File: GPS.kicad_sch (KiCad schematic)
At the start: 7 parts, among them Q1 BSS138, U46 2.54mm 2x6 socket

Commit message: Prepare v0.2
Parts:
- U13: footprint xtech:UM9XX_WitMotion -> local_Connectors:UM9XX_WitMotion Sabo
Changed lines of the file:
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@@
 	(title_block
 		(title "OpenMower SABO Mainboard for Series I & II")
-		(date "2025-02-26")
-		(rev "v0.1")
+		(date "2025-05-04")
+		(rev "v0.2")
 		(company "Apeheanger <joerg@ebeling.ws> for OpenMower")
 		(comment 1 "This design is licensed under CC BY-NC 4.0")
@@
 			)
 		)
-		(property "Footprint" "xtech:UM9XX_WitMotion"
+		(property "Footprint" "local_Connectors:UM9XX_WitMotion Sabo"
 			(at 184.15 107.95 0)
 			(effects
@@
 		(on_board yes)
 		(dnp no)
-		(fields_autoplaced yes)
 		(property "Reference" "Q1"
 			(at 166.37 106.6799 0)
@@
 		)
 		(property "Value" "BSS138"
-			(at 166.37 109.2199 0)
-			(effects
-				(font
+			(at 164.846 109.474 0)
+			(effects
+				(font

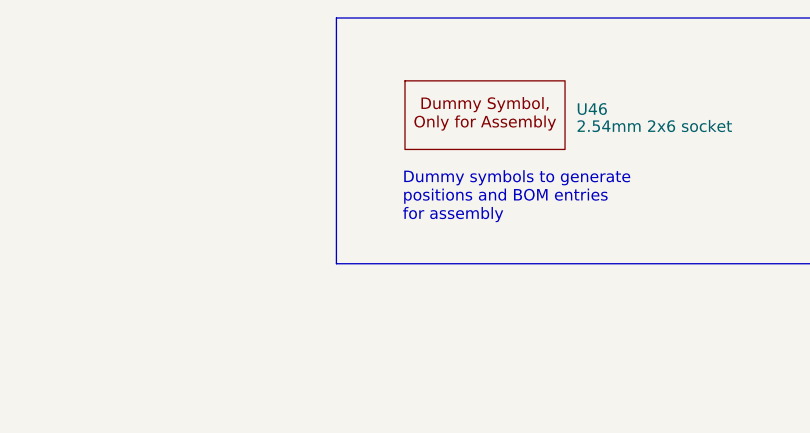
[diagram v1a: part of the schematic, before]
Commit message: Add RoHS Compliance Summary
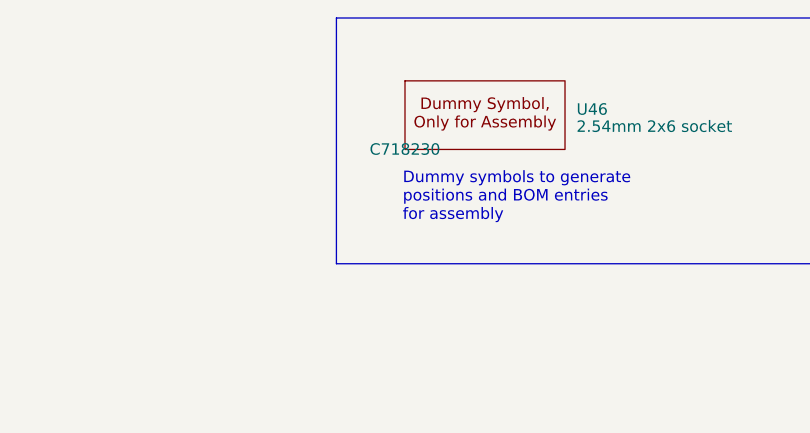
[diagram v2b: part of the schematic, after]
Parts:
- U46: JLC C718230 -> (none); LCSC Part # (none) -> C718230
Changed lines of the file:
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@@
+			)
+		)
+		(property "MPN" ""
+			(at 184.15 107.95 0)
+			(effects
+				(font
+					(size 1.27 1.27)
+				)
 			)
 		)
@@
 			)
 		)
+		(property "MPN" ""
+			(at 217.17 97.79 0)
+			(effects
+				(font
+					(size 1.27 1.27)
+				)
+			)
+		)
 		(pin "1"
 		)
@@
 			)
 		)
+		(property "MPN" ""
+			(at 139.7 115.57 0)
+			(effects
+				(font
+					(size 1.27 1.27)
+				)
+			)
+		)
 		(pin "1"
 		)
@@
 			)
 		)
+		(property "MPN" ""
+			(at 124.46 60.96 0)
+			(effects
+				(font
+					(size 1.27 1.27)
+				)
+			)
+		)
 		(pin "1"
 		)
@@
 			)
 		)
+		(property "MPN" ""
+			(at 147.32 107.95 0)
+			(effects
+				(font
+					(size 1.27 1.27)
+				)
+			)
+		)
 		(pin "1"
 		)
@@
 			)
 		)
-		(property "JLC" "C718230"
+		(property "JLC" ""
 			(at 354.33 31.75 0)
 			(effects
@@
 				)
 				(hide yes)
+			)
+		)
+		(property "MPN" ""
+			(at 354.33 31.75 0)
+			(effects
+				(font
+					(size 1.27 1.27)
+				)
+			)
+		)
+		(property "LCSC Part #" "C718230"
+			(at 354.33 31.75 0)
+			(effects
+				(font
+					(size 1.27 1.27)
+				)
 			)
 		)
@@
 			)
 		)
+		(property "MPN" ""
+			(at 160.02 107.95 0)
+			(effects
+				(font
+					(size 1.27 1.27)
+				)
+			)
+		)

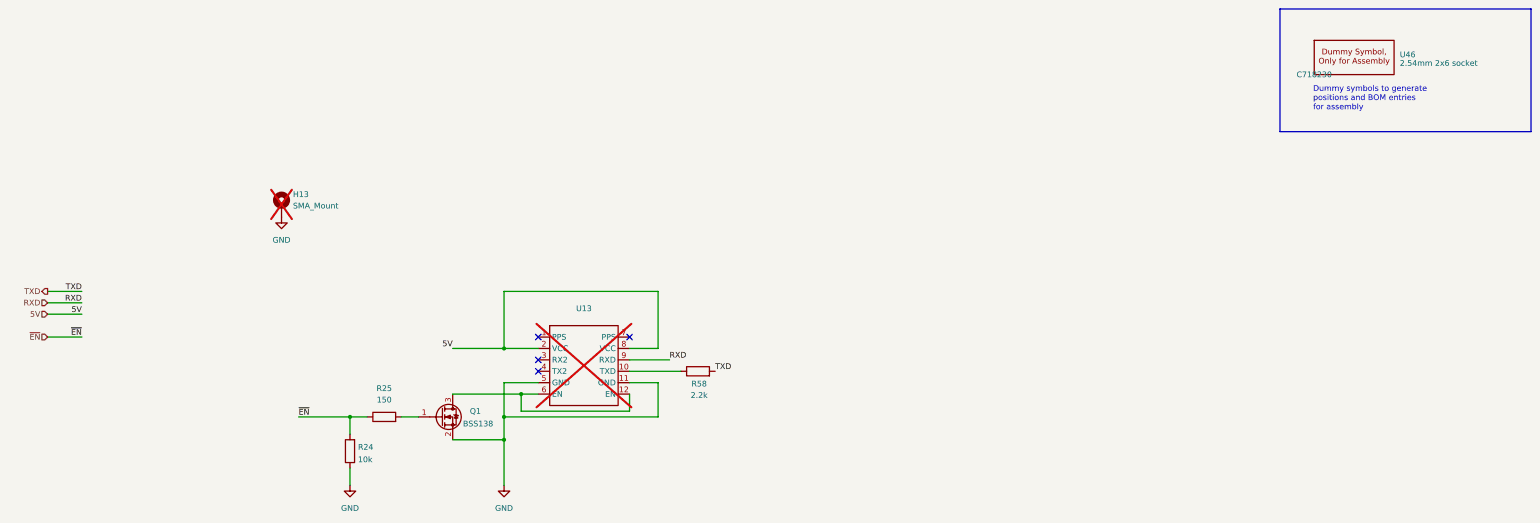
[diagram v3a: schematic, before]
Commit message: Restructured v0.1 for easier worktree use
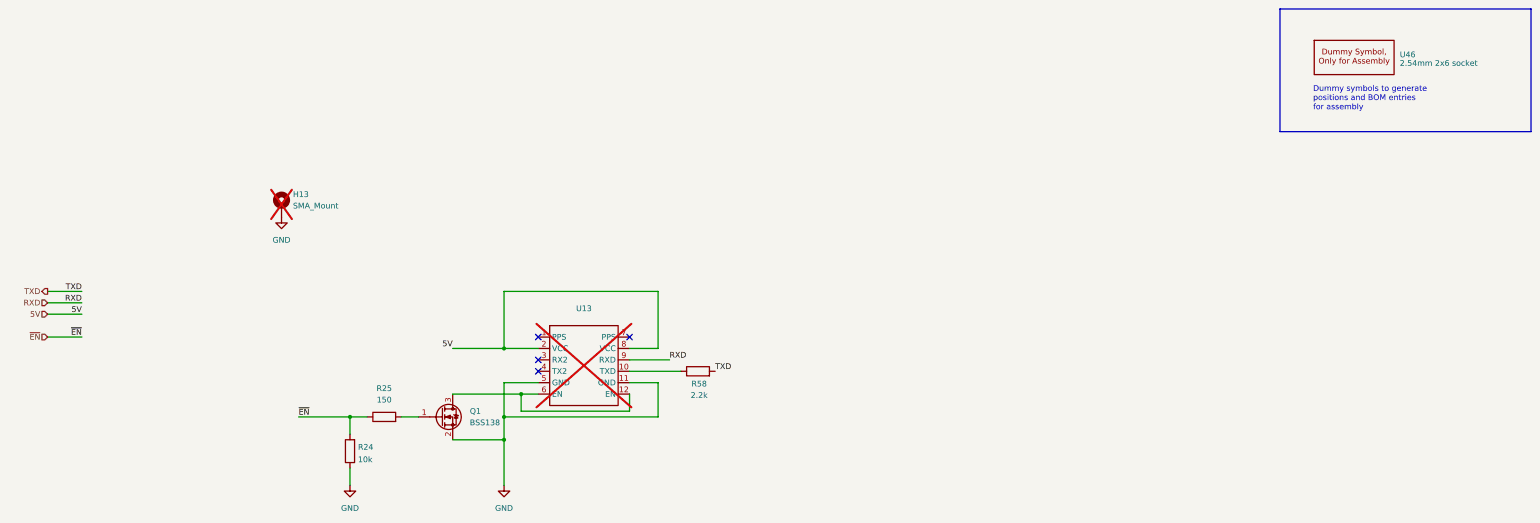
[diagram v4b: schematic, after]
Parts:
- U13: footprint local_Connectors:UM9XX_WitMotion Sabo -> xtech:UM9XX_WitMotion
- U46: JLC (none) -> C718230; LCSC Part # C718230 -> (none)
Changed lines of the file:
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@@
 	(title_block
 		(title "OpenMower SABO Mainboard for Series I & II")
-		(date "2025-05-22")
-		(rev "v0.2")
+		(date "2025-02-26")
+		(rev "v0.1")
 		(company "Apeheanger <joerg@ebeling.ws> for OpenMower")
 		(comment 1 "This design is licensed under CC BY-NC 4.0")
@@
 			)
 		)
-		(property "Footprint" "local_Connectors:UM9XX_WitMotion Sabo"
+		(property "Footprint" "xtech:UM9XX_WitMotion"
 			(at 184.15 107.95 0)
 			(effects
@@
 				)
 				(hide yes)
-			)
-		)
-		(property "MPN" ""
-			(at 184.15 107.95 0)
-			(effects
-				(font
-					(size 1.27 1.27)
-				)
 			)
 		)
@@
 			)
 		)
-		(property "MPN" ""
-			(at 217.17 97.79 0)
-			(effects
-				(font
-					(size 1.27 1.27)
-				)
-			)
-		)
 		(pin "1"
 		)
@@
 			)
 		)
-		(property "MPN" ""
-			(at 139.7 115.57 0)
-			(effects
-				(font
-					(size 1.27 1.27)
-				)
-			)
-		)
 		(pin "1"
 		)
@@
 			)
 		)
-		(property "MPN" ""
-			(at 124.46 60.96 0)
-			(effects
-				(font
-					(size 1.27 1.27)
-				)
-			)
-		)
 		(pin "1"
 		)
@@
 			)
 		)
-		(property "MPN" ""
-			(at 147.32 107.95 0)
-			(effects
-				(font
-					(size 1.27 1.27)
-				)
-			)
-		)
 		(pin "1"
 		)
@@
 			)
 		)
-		(property "JLC" ""
+		(property "JLC" "C718230"
 			(at 354.33 31.75 0)
 			(effects
@@
 				)
 				(hide yes)
-			)
-		)
-		(property "MPN" ""
-			(at 354.33 31.75 0)
-			(effects
-				(font
-					(size 1.27 1.27)
-				)
-			)
-		)
-		(property "LCSC Part #" "C718230"
-			(at 354.33 31.75 0)
-			(effects
-				(font
-					(size 1.27 1.27)
-				)
 			)
 		)
@@
 		(on_board yes)
 		(dnp no)
+		(fields_autoplaced yes)
 		(property "Reference" "Q1"
 			(at 166.37 106.6799 0)
@@
 		)
 		(property "Value" "BSS138"
-			(at 164.846 109.474 0)
+			(at 166.37 109.2199 0)
 			(effects
 				(font
@@
 			)
 		)
-		(property "MPN" ""
-			(at 160.02 107.95 0)
-			(effects
-				(font
-					(size 1.27 1.27)
-				)
-			)
-		)
